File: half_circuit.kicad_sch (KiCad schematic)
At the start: 20 parts, among them J11 Select, J13 Inh, J15 4046 Comp In, J17 4046 Out, J19 4040 Input, J21 4053 S3, J23 4053 C, J25 4053 C0 C1, J27 4040 Output, J29 4017 Fdbk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

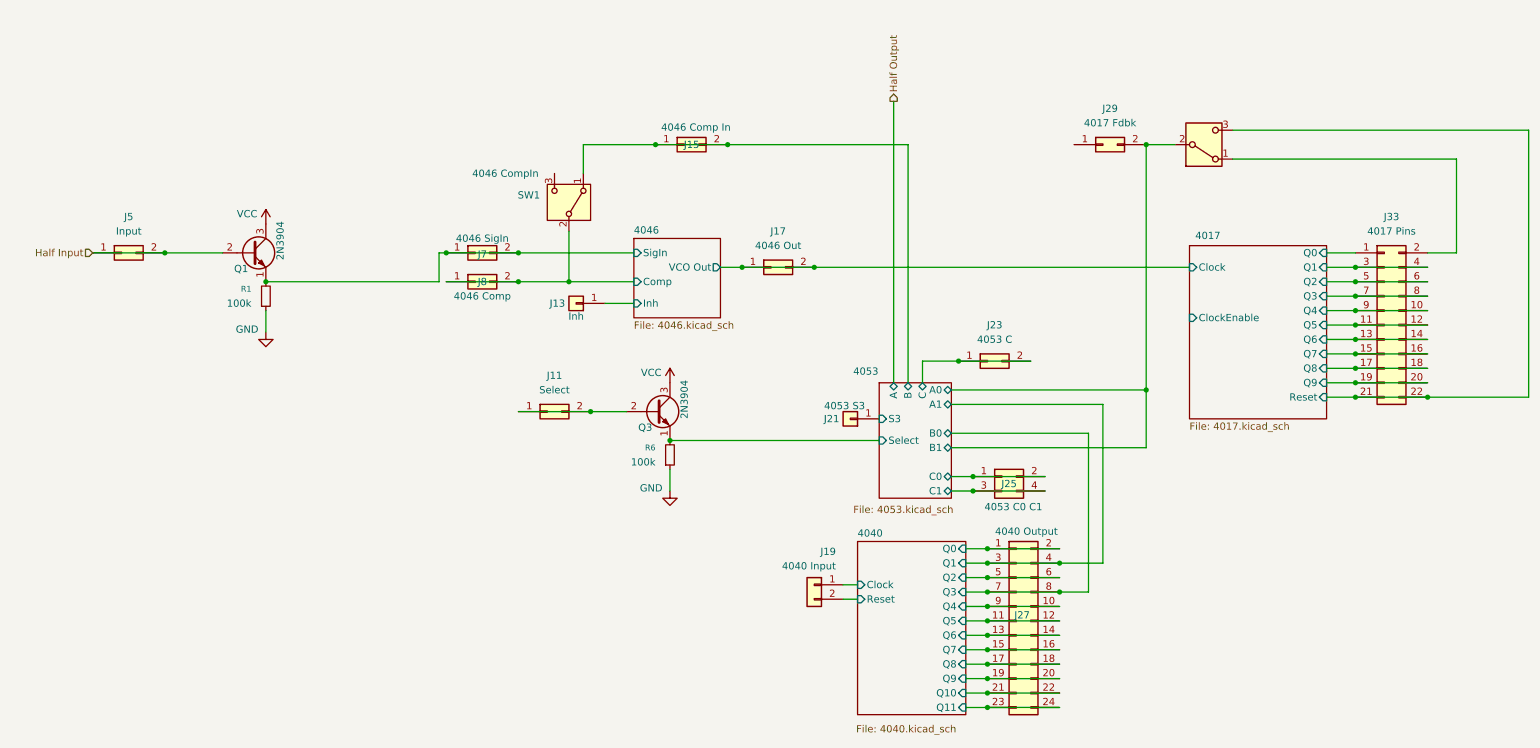
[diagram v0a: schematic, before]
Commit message: two halves routing
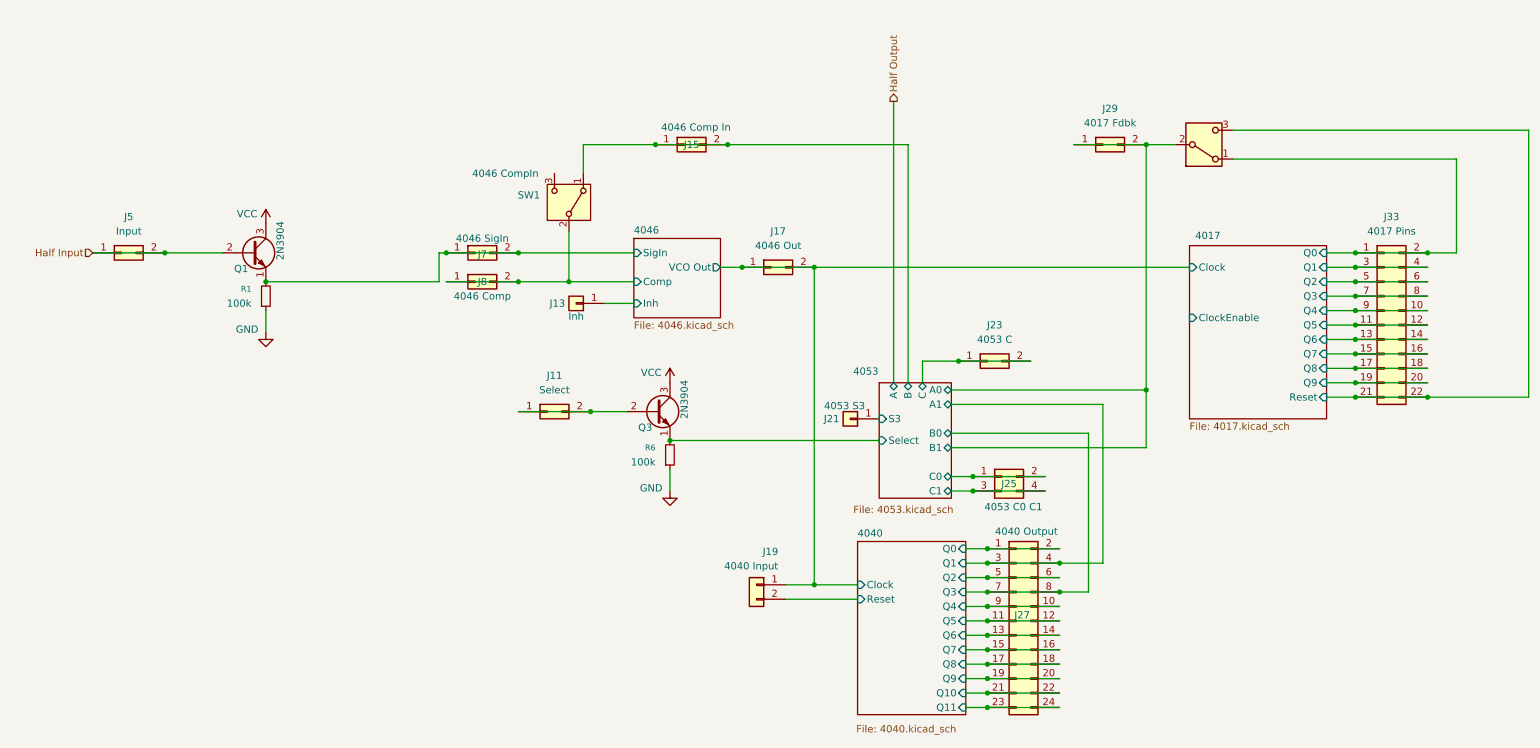
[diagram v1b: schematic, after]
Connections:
- net 4040/Clock is gone; now on net 4017/Clock: J19.1 (Pin_1)
- net 4017/Q0: now also J33.2 (Pin_2), SW3.1 (A)
- net 4053/A0: now also J29.1 (Pin_1)
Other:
- moved on the sheet: J19
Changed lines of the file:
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@@
 	)
 	(junction
+		(at 152.4 119.38)
+		(diameter 0)
+		(color 0 0 0 0)
+	)
+	(junction
 		(at 100.33 60.96)
 		(diameter 0)
@@
 	)
 	(junction
+		(at 260.35 60.96)
+		(diameter 0)
+		(color 0 0 0 0)
+	)
+	(junction
+		(at 247.65 60.96)
+		(diameter 0)
+		(color 0 0 0 0)
+	)
+	(junction
 		(at 109.22 66.04)
 		(diameter 0)
@@
 	(wire
 		(pts
+			(xy 247.65 60.96) (xy 260.35 60.96)
+		)
+		(stroke
+			(width 0)
+			(type default)
+		)
+	)
+	(wire
+		(pts
 			(xy 260.35 86.36) (xy 278.13 86.36)
 		)
@@
 	(wire
 		(pts
+			(xy 152.4 63.5) (xy 152.4 119.38)
+		)
+		(stroke
+			(width 0)
+			(type default)
+		)
+	)
+	(wire
+		(pts
 			(xy 179.07 135.89) (xy 182.88 135.89)
 		)
@@
 	(wire
 		(pts
+			(xy 198.12 41.91) (xy 210.82 41.91)
+		)
+		(stroke
+			(width 0)
+			(type default)
+		)
+	)
+	(wire
+		(pts
 			(xy 247.65 86.36) (xy 260.35 86.36)
 		)
@@
 	(wire
 		(pts
+			(xy 152.4 119.38) (xy 160.02 119.38)
+		)
+		(stroke
+			(width 0)
+			(type default)
+		)
+	)
+	(wire
+		(pts
 			(xy 247.65 78.74) (xy 260.35 78.74)
 		)
@@
 	(wire
 		(pts
-			(xy 157.48 121.92) (xy 160.02 121.92)
+			(xy 147.32 121.92) (xy 160.02 121.92)
 		)
 		(stroke
@@
 	(wire
 		(pts
-			(xy 157.48 119.38) (xy 160.02 119.38)
+			(xy 147.32 119.38) (xy 152.4 119.38)
 		)
 		(stroke
@@
 	(symbol
 		(lib_id "Connector_Generic:Conn_01x02")
-		(at 152.4 119.38 0)
+		(at 142.24 119.38 0)
 		(mirror y)
 		(unit 1)
@@
 		(dnp no)
 		(property "Reference" "J19"
-			(at 156.21 113.538 0)
+			(at 146.05 113.538 0)
 			(effects
 				(font
@@
 		)
 		(property "Value" "4040 Input"
-			(at 156.21 116.078 0)
+			(at 146.05 116.078 0)
 			(effects
 				(font
@@
 		)
 		(property "Footprint" "Connector_PinHeader_2.54mm:PinHeader_1x02_P2.54mm_Vertical"
-			(at 152.4 119.38 0)
+			(at 142.24 119.38 0)
 			(effects
 				(font
@@
 		)
 		(property "Datasheet" "~"
-			(at 152.4 119.38 0)
+			(at 142.24 119.38 0)
 			(effects
 				(font
@@
 		)
 		(property "Description" "Generic connector, single row, 01x02, script generated (kicad-library-utils/schlib/autogen/connector/)"
-			(at 152.4 119.38 0)
+			(at 142.24 119.38 0)
 			(effects
 				(font
@@
 			)
 		)
-		(instances)
 	)
 	(sheet
@@
 			)
 		)
-		(instances)
 	)
 	(sheet
@@
 			)
 		)
-		(instances)
 	)
 	(sheet
@@
 			)
 		)
-		(instances)
 	)
 )
